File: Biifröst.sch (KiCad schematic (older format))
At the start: 15 parts, among them J1 Pitaya_Go, J2 LCD_SPI, J3 SPI_SD, J4 CMSIS-DAP, J5 DEBUG UART *DNP*, SW1 JS1400AFQ, SW2 TL9100AF200Q, SW3 TL9100AF200Q

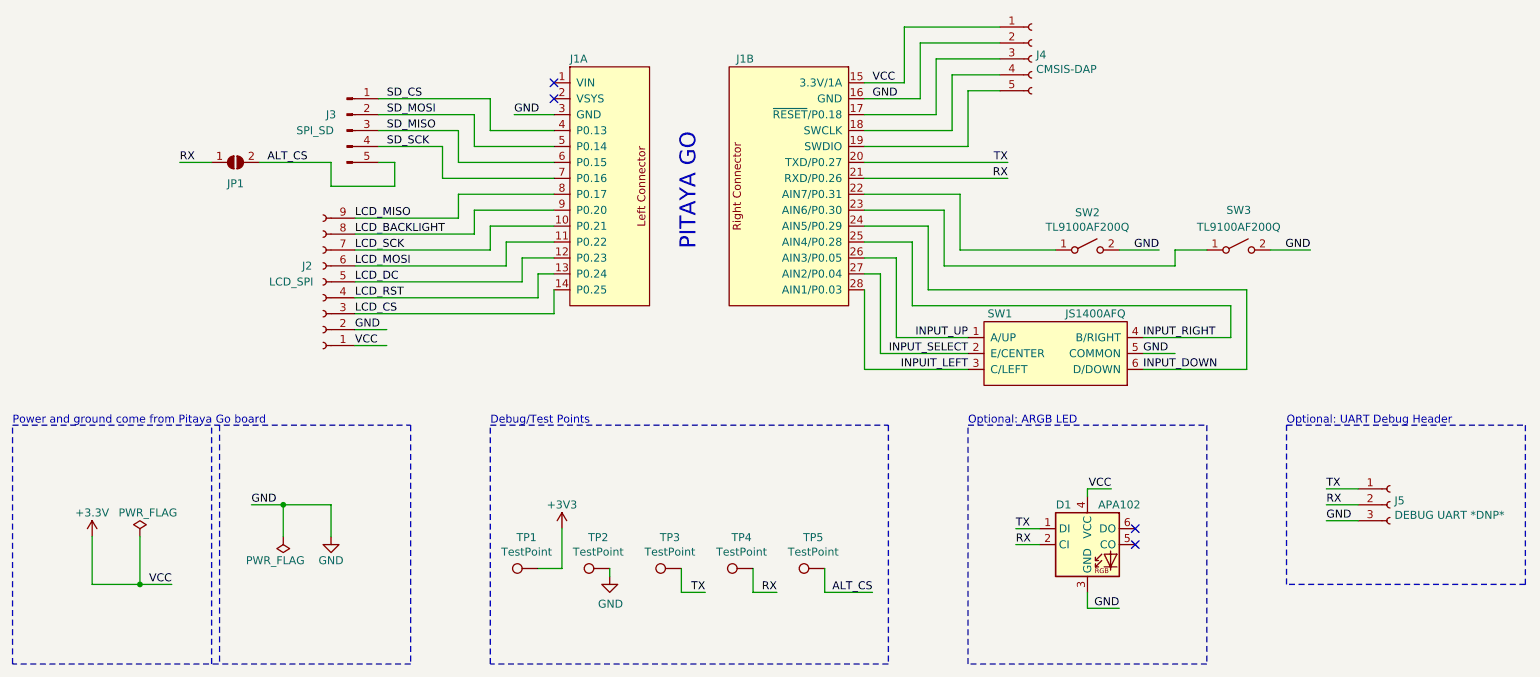
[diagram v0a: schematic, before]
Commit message: Update pins to have not bars where they should be.
And fixed a dumb typo on a net name.
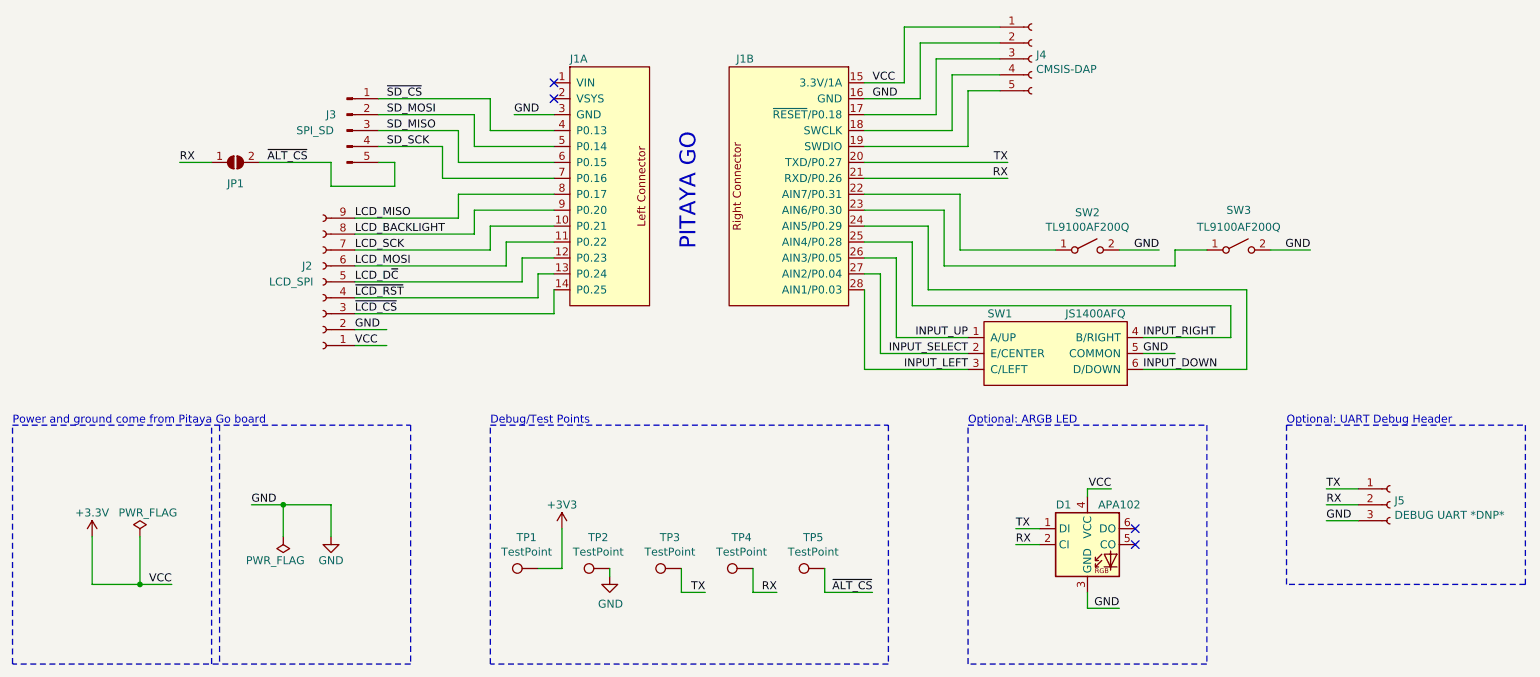
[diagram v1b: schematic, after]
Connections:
- net ALT_CS renamed ~ALT_CS~
- net INPUIT_LEFT renamed INPUT_LEFT
- net LCD_CS renamed ~LCD_CS~
- net LCD_DC renamed LCD_D~C~
- net LCD_RST renamed ~LCD_RST~
- net SD_CS renamed ~SD_CS~
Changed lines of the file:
@@
 GND
 Text Label 3350 2950 0    50   ~ 0
-SD_CS
+~SD_CS~
 Text Label 3350 3050 0    50   ~ 0
 SD_MOSI
@@
 SD_SCK
 Text Label 2600 3350 0    50   ~ 0
-ALT_CS
+~ALT_CS~
 Text Label 3150 3700 0    50   ~ 0
 LCD_MISO
@@
 LCD_MOSI
 Text Label 3150 4100 0    50   ~ 0
-LCD_DC
+LCD_D~C~
 Text Label 3150 4200 0    50   ~ 0
-LCD_RST
+~LCD_RST~
 Text Label 3150 4300 0    50   ~ 0
-LCD_CS
+~LCD_CS~
 Text Label 3150 4400 0    50   ~ 0
 GND
@@
 INPUT_SELECT
 Text Label 7000 4650 2    50   ~ 0
-INPUIT_LEFT
+INPUT_LEFT
 Text Label 8100 4450 0    50   ~ 0
 INPUT_RIGHT
@@
 	6100 6050 6400 6050
 Text Label 6400 6050 2    50   ~ 0
-ALT_CS
+~ALT_CS~
 Text Label 2050 3350 0    50   ~ 0
 RX

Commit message: Add VIN/VSYS breakout. Add 4 hole cuts that will line up with sister boards.
2 hole cuts will align with the pitaya go holes (1 top, 1 bottom, on one side)
2 hole cuts will align with the LCD board holes (1 top, 1 bottom, opposite side from pitaya.)

Not perfectly ideal, but required no trace moves, and they may be useful.
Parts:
- added J6: OPT PWR *DNP*, Connector_PinHeader_2.54mm:PinHeader_1x03_P2.54mm_Horizontal, symbol Connector:Conn_01x03_Female
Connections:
- net GND: now also J6.3 (Pin_3)
- net VIN: now reaches J1.1 (VIN)
- net VIN: now also J6.1 (Pin_1)
- net VSYS: now reaches J1.2 (VSYS)
- net VSYS: now also J6.2 (Pin_2)
- no-connect marks 4 -> 2
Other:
- note added: "Optional: \nVIN (4.5-6.4V) (IN)\nVSYS (4.4V/2A) (OUT)"
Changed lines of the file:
@@
 Text Label 2050 3350 0    50   ~ 0
 RX
-NoConn ~ 4400 2950
-NoConn ~ 4400 2850
 Wire Wire Line
 	4750 5900 4750 5950
@@
 $EndComp
 Wire Wire Line
-	1500 6000 1500 5700
+	1500 5650 1500 5350
 Wire Wire Line
-	1800 6000 1800 5700
+	1800 5650 1800 5350
 $Comp
 L power:PWR_FLAG #FLG0102
 U 1 1 5F2C8299
-P 1800 5700
-F 0 "#FLG0102" H 1800 5775 50  0001 C CNN
-F 1 "PWR_FLAG" H 1850 5850 50  0000 C CNN
-F 2 "" H 1800 5700 50  0001 C CNN
-F 3 "~" H 1800 5700 50  0001 C CNN
-	1    1800 5700
+P 1800 5350
+F 0 "#FLG0102" H 1800 5425 50  0001 C CNN
+F 1 "PWR_FLAG" H 1850 5500 50  0000 C CNN
+F 2 "" H 1800 5350 50  0001 C CNN
+F 3 "~" H 1800 5350 50  0001 C CNN
+	1    1800 5350
 	1    0    0    -1
 $EndComp
 Wire Wire Line
-	2000 6000 1800 6000
-Connection ~ 1800 6000
+	2000 5650 1800 5650
+Connection ~ 1800 5650
 Wire Wire Line
-	1800 6000 1500 6000
-Text Label 2000 6000 2    50   ~ 0
+	1800 5650 1500 5650
+Text Label 2000 5650 2    50   ~ 0
 VCC
 $Comp
 L power:+3.3V #PWR0101
 U 1 1 5F2D92AD
-P 1500 5700
-F 0 "#PWR0101" H 1500 5550 50  0001 C CNN
-F 1 "+3.3V" H 1500 5850 50  0000 C CNN
-F 2 "" H 1500 5700 50  0001 C CNN
-F 3 "" H 1500 5700 50  0001 C CNN
-	1    1500 5700
+P 1500 5350
+F 0 "#PWR0101" H 1500 5200 50  0001 C CNN
+F 1 "+3.3V" H 1500 5500 50  0000 C CNN
+F 2 "" H 1500 5350 50  0001 C CNN
+F 3 "" H 1500 5350 50  0001 C CNN
+	1    1500 5350
 	1    0    0    -1
 $EndComp
@@
 Text Notes 4000 5000 0    50   ~ 0
 Debug/Test Points
+Wire Notes Line
+	1000 5750 2250 5750
+Text Notes 1050 6000 0    50   ~ 0
+Optional: \nVIN (4.5-6.4V) (IN)\nVSYS (4.4V/2A) (OUT)
+$Comp
+L Connector:Conn_01x03_Female J6
+U 1 1 5F40CEEA
+P 1550 6250
+F 0 "J6" H 1578 6276 50  0000 L CNN
+F 1 "OPT PWR *DNP*" H 1578 6185 50  0000 L CNN
+F 2 "Connector_PinHeader_2.54mm:PinHeader_1x03_P2.54mm_Horizontal" H 1550 6250 50  0001 C CNN
+F 3 "~" H 1550 6250 50  0001 C CNN
+	1    1550 6250
+	1    0    0    -1
+$EndComp
+Wire Wire Line
+	4400 2850 4150 2850
+Wire Wire Line
+	4400 2950 4150 2950
+Text Label 4150 2850 0    50   ~ 0
+VIN
+Text Label 4150 2950 0    50   ~ 0
+VSYS
+Wire Wire Line
+	1350 6350 1100 6350
+Text Label 1100 6350 0    50   ~ 0
+GND
+Wire Wire Line
+	1350 6150 1100 6150
+Wire Wire Line
+	1350 6250 1100 6250
+Text Label 1100 6150 0    50   ~ 0
+VIN
+Text Label 1100 6250 0    50   ~ 0
+VSYS
 $EndSCHEMATC
